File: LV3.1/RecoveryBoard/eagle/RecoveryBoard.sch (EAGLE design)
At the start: 88 parts, among them IC1 BD62120AEFJ-E2, Q6 MOSFET-PCH-SOT23-6, U1 STM32F042K6, U10 TPS63070, Y1 ECS-160-10-36Q-ES-TR

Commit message: OCD on package sizes 0603 for normal caps and resistors; 0805 for large caps, and larger yet for larger caps.
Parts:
- C1, C18, C19, C20, C3, C4: device rcl:C-EUC0402 -> oresat-rcl:C-EU0603-C-NOSILK
- C10, C28, C6, C9: device oresat-rcl:C-EU0805-B-NOSILK -> oresat-rcl:C-EU0805-C-NOSILK
- C17: device oresat-rcl:C-EU0603-C-NOSILK -> oresat-rcl:C-EU0805-C-NOSILK
- C5, C8: device oresat-rcl:C-EU0603-B-NOSILK -> oresat-rcl:C-EU0805-C-NOSILK
- C7: device rcl_custom:C-EU0402-B-NOSILK -> oresat-rcl:C-EU0603-C-NOSILK
- R1, R2, R3, R4, R5, R6: device rcl_custom:R-US_0402-B-NOSILK -> oresat-rcl:R-US_0603-C-NOSILK
- R10, R11, R12, R13, R14, R26, R27, R28, R29, R32, R33, R34, R35, R36, R7, R8, R9: device rcl:R-US_R0402 -> oresat-rcl:R-US_0603-C-NOSILK
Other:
- note removed: "0603"

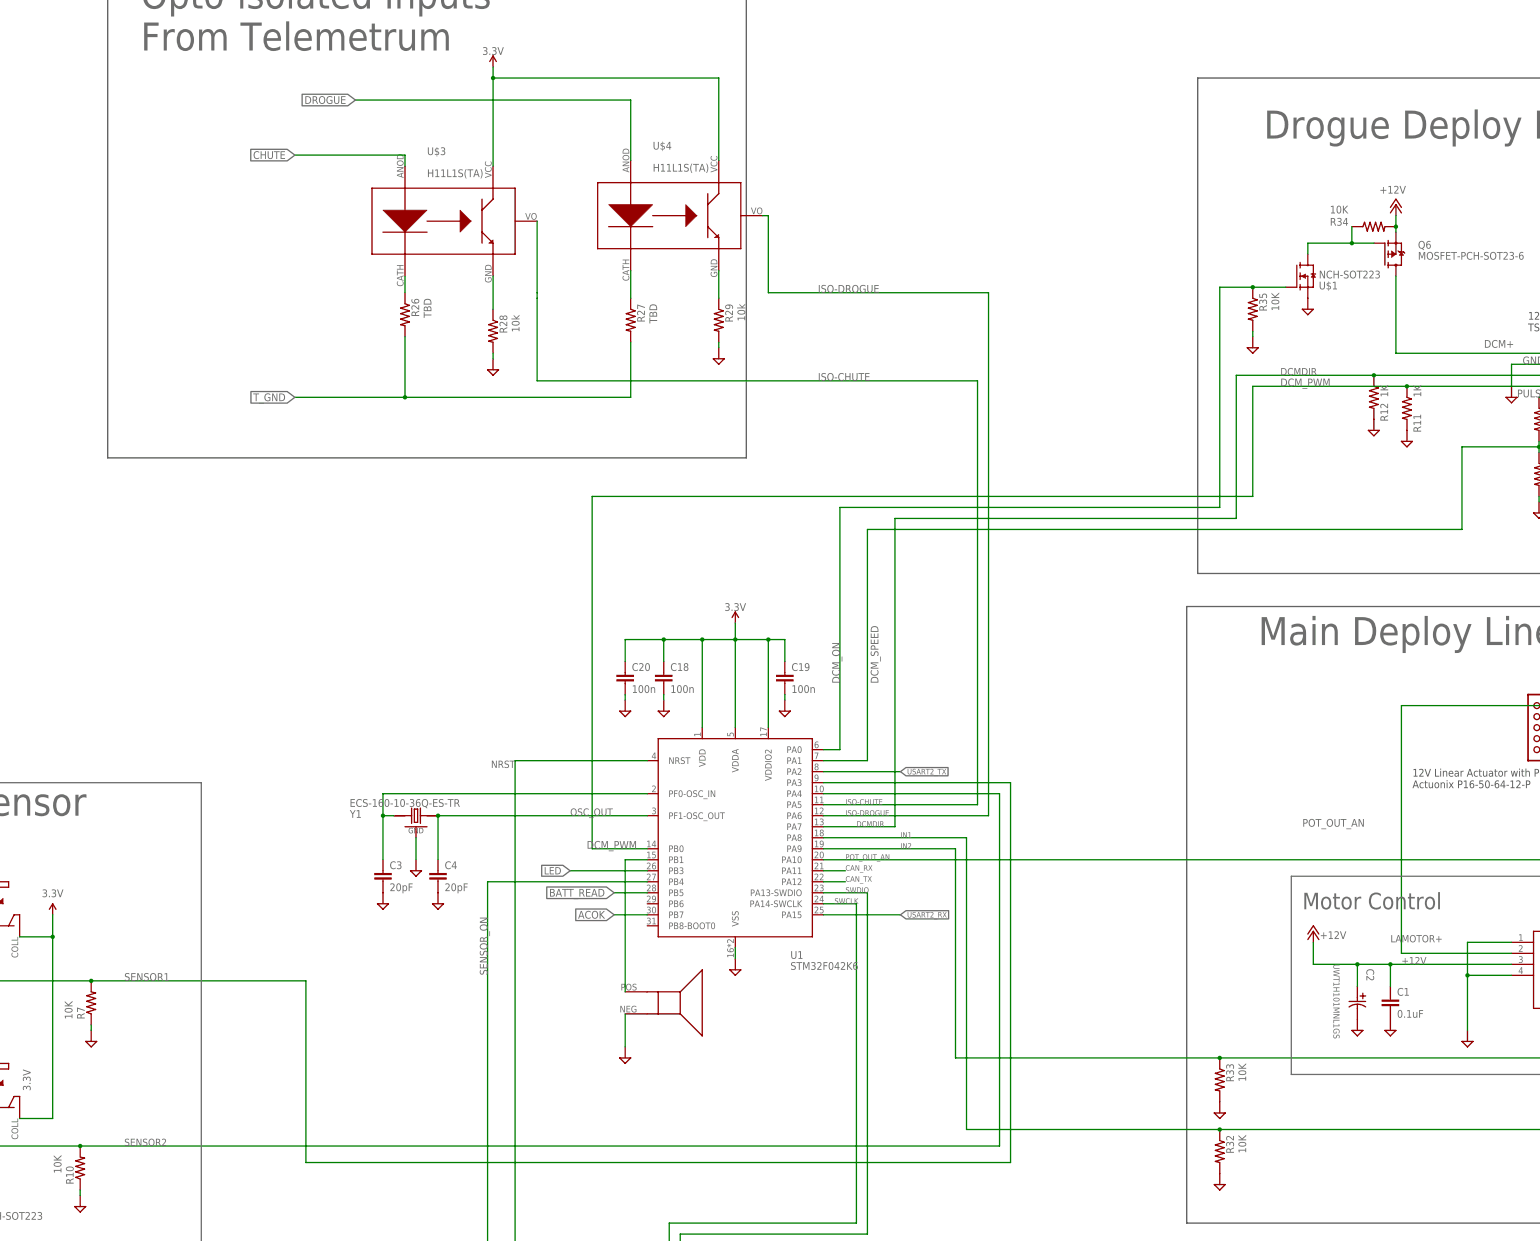
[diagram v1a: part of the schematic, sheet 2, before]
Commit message: beginning routing and placement
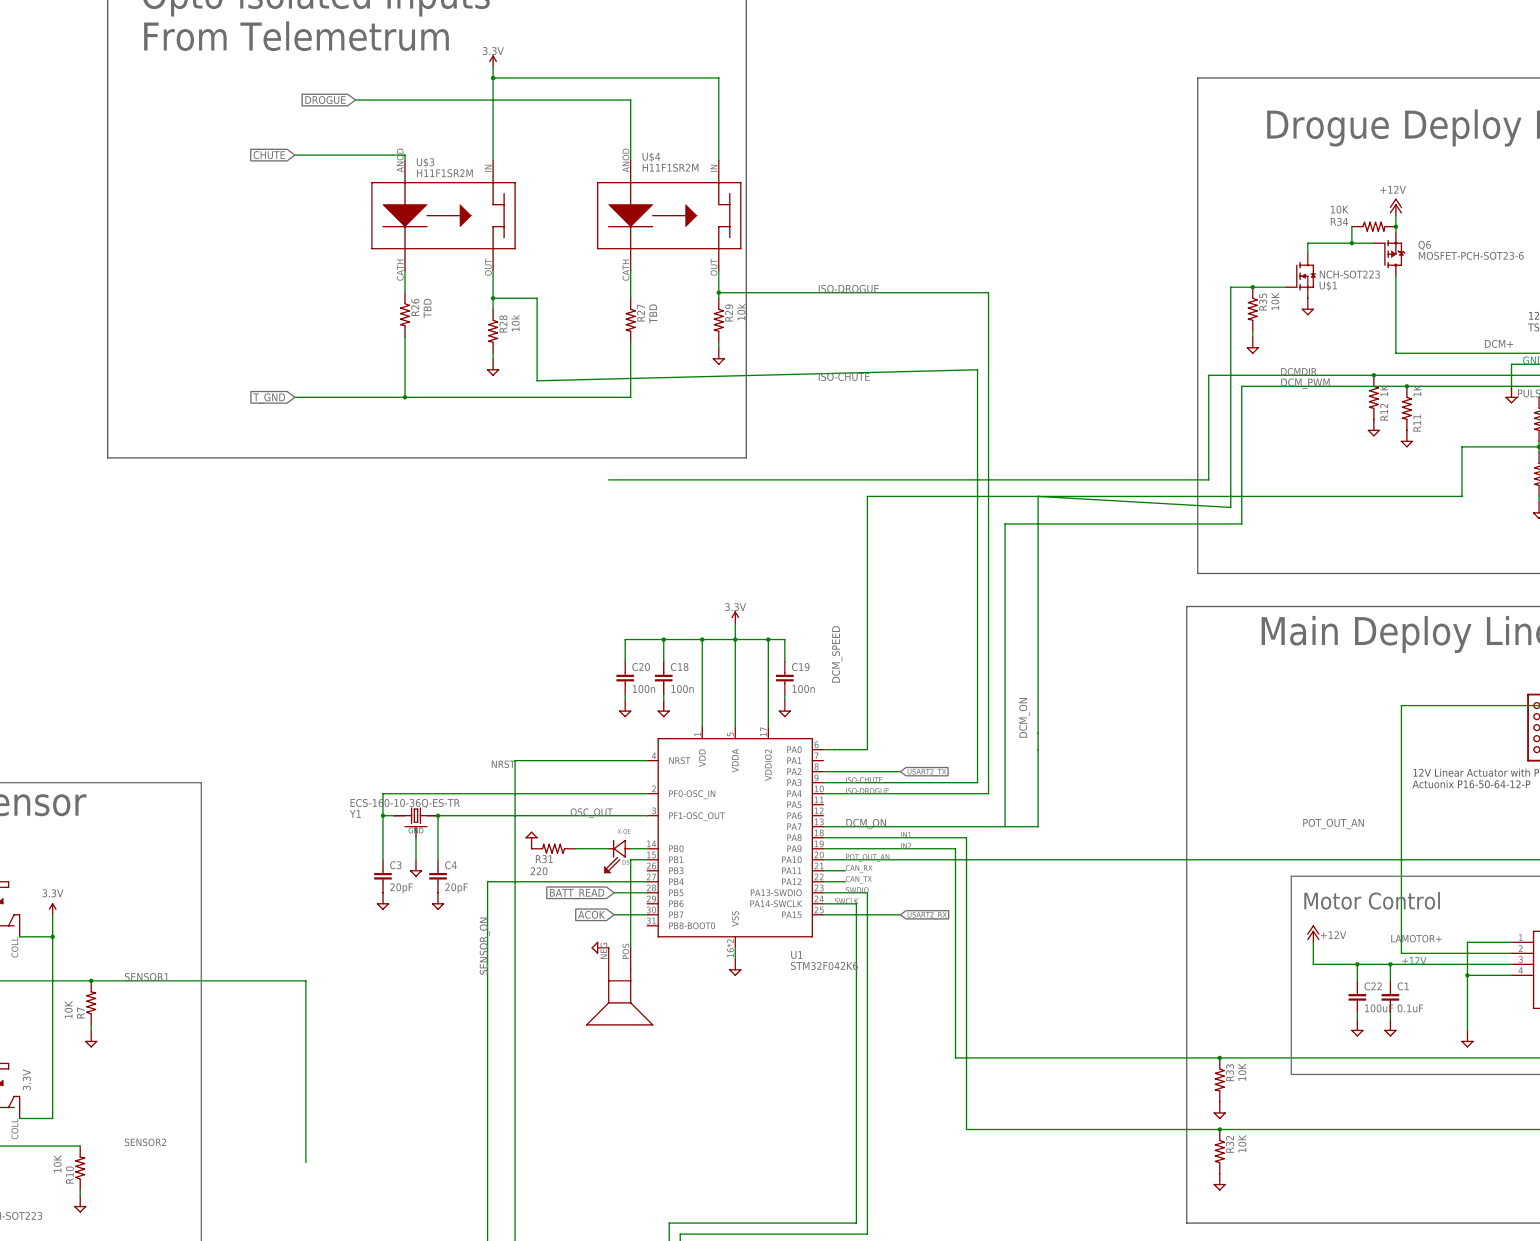
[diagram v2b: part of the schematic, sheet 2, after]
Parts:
- removed C2: UWT1H101MNL1GS, UWT1H101MNL1GS:UWT1H101MNL1GS
- added C22: 100uF, oresat-rcl:C-EUC1206
- added D5: X-QE, D-Cree-XQE-LED:X-QE
- added R31: 220, oresat-rcl:R-US_0603-C-NOSILK
- U$3, U$4: value H11L1S(TA) -> H11F1SR2M; device Q--H11L1S(TA)--OptoIsolator:H11L1S(TA) -> Q--H11F1SR2M--OptoIsolator:H11F1SR2M
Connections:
- removed net LED: U1.PB3
- removed net N$25: R28.1, U$3.EMIT
- removed net N$29: R29.1, U$4.EMIT
- new net N$15: D5.A, U1.PB0
- new net N$4: D5.C, R31.1
- net +12V: now also C22.1; no longer C2.1
- net 3.3V: now also U$3.IN, U$4.IN; no longer U$3.COLL, U$4.COLL
- net ARM-IN: now also JP2.2; no longer JP2.6
- net ARM-OUT: now also JP2.1; no longer JP2.7
- net CHUTE: now also JP2.5; no longer JP2.3
- net DCMDIR: no longer U1.PA7
- net DCM_ON: now also U1.PA7; no longer U1.PA0
- net DCM_PWM: no longer U1.PB0
- net DCM_SPEED: now also U1.PA0; no longer U1.PA1
- net DROGUE: now also JP2.6; no longer JP2.4
- net GND: now also C22.2, JP2.4, R31.2; no longer C2.2, JP2.2
- net ISO-CHUTE: now also R28.1, U$3.OUT, U1.PA3; no longer U$3.OUTPUT, U1.PA5
- net ISO-DROGUE: now also R29.1, U$4.OUT, U1.PA4; no longer U$4.OUTPUT, U1.PA6
- net SENSOR1: no longer U1.PA3
- net SENSOR2: no longer U1.PA4
- net T_GND: now also JP2.7; no longer JP2.5
- net VUMB: now also JP2.3; no longer JP2.1
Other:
- note removed: "ARM 1"
- note removed: "ARM 2"
- moved on the sheet: C1
